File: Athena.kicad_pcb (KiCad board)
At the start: 2 copper layers, 60 x 80 mm, 81 parts, among them J1 LUM 1503-09, J2 LUM 1503-09, J3 LUM 1503-09, J4 NRJ6HF, J5 DC BU21 90, SW1 MS 500FVT, U1 NE5532, U2 TL072, U3 OPA2134, U4 NE5532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

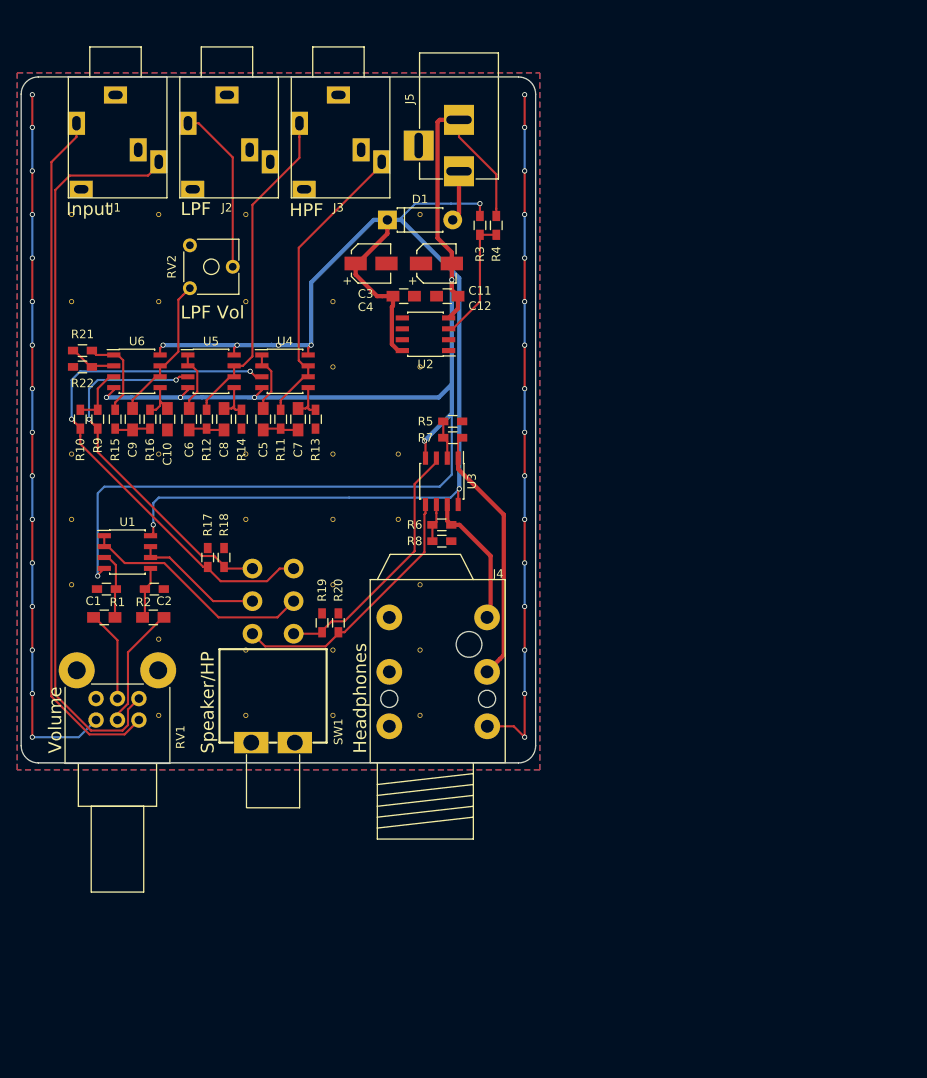
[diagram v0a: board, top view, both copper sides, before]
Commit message: changed enclosure, added power leds, resized pcb
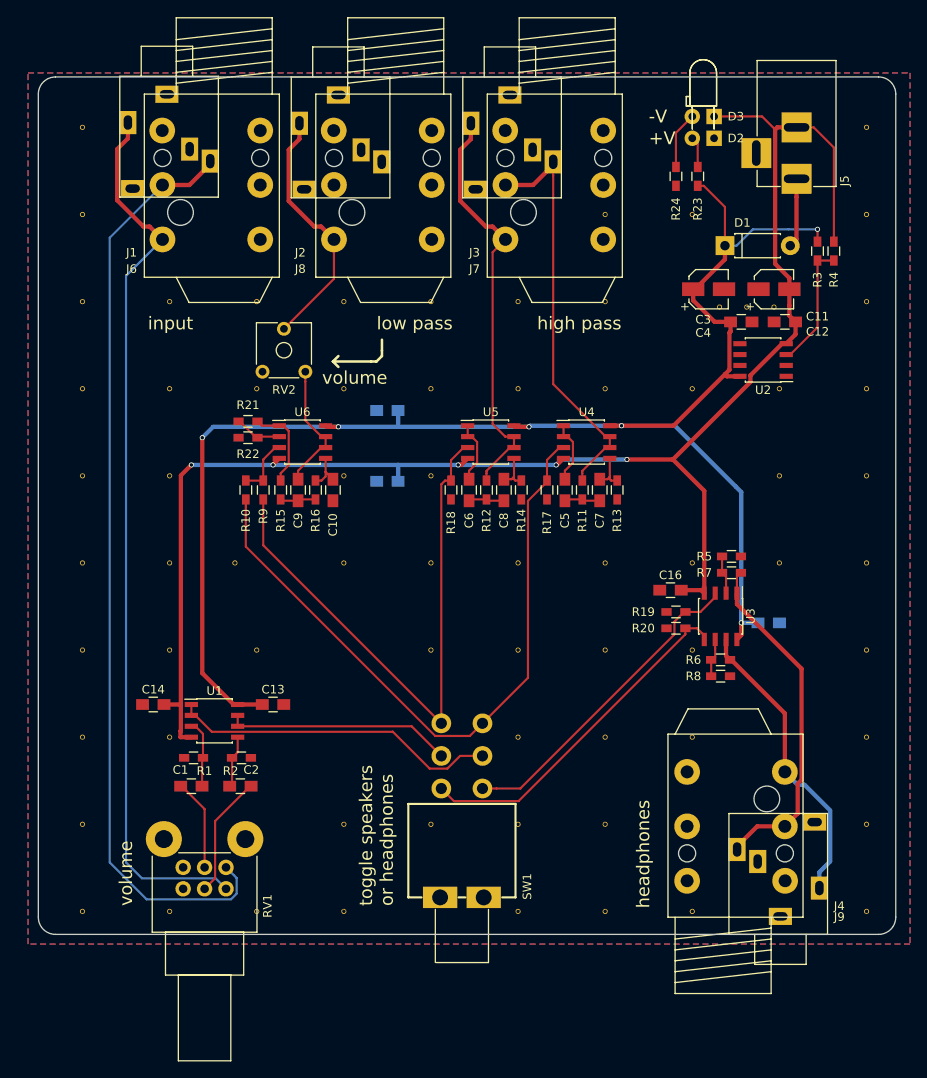
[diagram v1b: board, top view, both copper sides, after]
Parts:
- removed the REF*** at (47.0, 72.4)
- removed the V30 at (52.1, 109.2)
- added C13: 100n, Capacitors_SMD:C_0805_HandSoldering, F.Cu at (65.4, 108.0)
- added C14: 100n, Capacitors_SMD:C_0805_HandSoldering, F.Cu at (51.4, 108.0)
- added C15: 100n, Capacitors_SMD:C_0805_HandSoldering, B.Cu at (123.2, 98.4)
- added C16: 100n, Capacitors_SMD:C_0805_HandSoldering, F.Cu at (111.8, 94.6)
- added C17: 100n, Capacitors_SMD:C_0805_HandSoldering, B.Cu at (78.7, 73.7)
- added C18: 100n, Capacitors_SMD:C_0805_HandSoldering, B.Cu at (78.7, 81.9)
- added D2: LED, LEDs:LED_D3.0mm_Horizontal_O3.81mm_Z6.0mm, F.Cu at (116.8, 41.9)
- added D3: LED, LEDs:LED_D3.0mm_Horizontal_O1.27mm_Z2.0mm, F.Cu at (116.8, 39.4)
- added J6: NRJ6HF, NRJ6HF:NRJ6HF, F.Cu at (59.7, 36.8)
- added J7: NRJ6HF, NRJ6HF:NRJ6HF, F.Cu at (99.7, 36.8)
- added J8: NRJ6HF, NRJ6HF:NRJ6HF, F.Cu at (79.7, 36.8)
- added J9: LUM 1503-09, Lumberg:LUM1503-09, F.Cu at (124.6, 134.8)
- added R23: 330R, Resistors_SMD:R_0603_HandSoldering, F.Cu at (114.9, 46.4)
- added R24: 330R, Resistors_SMD:R_0603_HandSoldering, F.Cu at (112.4, 46.4)
- added REF***: OSHW-Logo2_14.6x12mm_SilkScreen, Symbols:OSHW-Logo2_14.6x12mm_SilkScreen, B.Cu at (88.0, 84.8)
- added V30: VIA, via:VIA-0.6, F.Cu at (43.2, 40.6)
- added V30: VIA, via:VIA-0.6, F.Cu at (134.6, 101.6)
- added V30: VIA, via:VIA-0.6, F.Cu at (134.6, 91.4)
- added V30: VIA, via:VIA-0.6, F.Cu at (124.5, 91.4)
- added V30: VIA, via:VIA-0.6, F.Cu at (43.2, 50.8)
- added V30: VIA, via:VIA-0.6, F.Cu at (104.1, 50.8)
- added V30: VIA, via:VIA-0.6, F.Cu at (114.3, 50.8)
- added V30: VIA, via:VIA-0.6, F.Cu at (134.6, 40.6)
- added V30: VIA, via:VIA-0.6, F.Cu at (134.6, 50.8)
- added V30: VIA, via:VIA-0.6, F.Cu at (134.6, 61.0)
- added V30: VIA, via:VIA-0.6, F.Cu at (134.6, 71.1)
- added V30: VIA, via:VIA-0.6, F.Cu at (134.6, 81.3)
- added V31: VIA, via:VIA-0.6, F.Cu at (43.2, 101.6)
- added V32: VIA, via:VIA-0.6, F.Cu at (53.3, 101.6)
- added V33: VIA, via:VIA-0.6, F.Cu at (63.5, 101.6)
- added V34: VIA, via:VIA-0.6, F.Cu at (83.8, 101.6)
- added V35: VIA, via:VIA-0.6, F.Cu at (94.0, 101.6)
- added V36: VIA, via:VIA-0.6, F.Cu at (104.1, 101.6)
- added V37: VIA, via:VIA-0.6, F.Cu at (114.3, 101.6)
- added V38: VIA, via:VIA-0.6, F.Cu at (43.2, 111.8)
- added V39: VIA, via:VIA-0.6, F.Cu at (53.3, 111.8)
- added V40: VIA, via:VIA-0.6, F.Cu at (117.5, 61.6)
- added V41: VIA, via:VIA-0.6, F.Cu at (120.7, 61.6)
- added V42: VIA, via:VIA-0.6, F.Cu at (94.0, 111.8)
- added V43: VIA, via:VIA-0.6, F.Cu at (104.1, 111.8)
- added V44: VIA, via:VIA-0.6, F.Cu at (114.3, 111.8)
- added V45: VIA, via:VIA-0.6, F.Cu at (123.8, 61.6)
- added V46: VIA, via:VIA-0.6, F.Cu at (43.2, 121.9)
- added V47: VIA, via:VIA-0.6, F.Cu at (73.7, 121.9)
- added V48: VIA, via:VIA-0.6, F.Cu at (83.8, 121.9)
- added V49: VIA, via:VIA-0.6, F.Cu at (94.0, 121.9)
- added V50: VIA, via:VIA-0.6, F.Cu at (104.1, 121.9)
- added V51: VIA, via:VIA-0.6, F.Cu at (43.2, 132.1)
- added V52: VIA, via:VIA-0.6, F.Cu at (53.3, 132.1)
- added V53: VIA, via:VIA-0.6, F.Cu at (63.5, 132.1)
- added V54: VIA, via:VIA-0.6, F.Cu at (73.7, 132.1)
- added V55: VIA, via:VIA-0.6, F.Cu at (94.0, 132.1)
- added V56: VIA, via:VIA-0.6, F.Cu at (104.1, 132.1)
- added V57: VIA, via:VIA-0.6, F.Cu at (114.3, 132.1)
- added V58: VIA, via:VIA-0.6, F.Cu at (134.6, 132.1)
- added V59: VIA, via:VIA-0.6, F.Cu at (134.6, 121.9)
- added V60: VIA, via:VIA-0.6, F.Cu at (134.6, 111.8)
- moved V29 73.0 mm to (124.5, 71.1)
- moved V28 65.5 mm to (124.5, 81.3)
- moved V7 65.3 mm to (104.1, 61.0)
- moved V26 49.6 mm to (114.3, 71.1)
- moved V12 47.7 mm to (83.8, 71.1)
- moved V27 45.5 mm to (114.3, 91.4)
- moved REF*** 43.8 mm to (88.0, 96.5)
- moved V15 41.4 mm to (43.2, 81.3)
- moved R19 41.3 mm to (112.4, 97.2), turned to 180 degrees
- moved R17 40.3 mm to (97.4, 82.9), turned to 270 degrees
- moved C11 39.5 mm to (123.8, 59.5)
- moved C12 39.5 mm to (125.1, 63.3)
- moved C3 39.5 mm to (116.2, 59.5)
- moved C4 39.5 mm to (120.0, 63.3)
- moved D1 39.5 mm to (118.1, 54.4)
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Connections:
- J2 pad 2: (no net) -> Net-(J2-Pad2)
- J2 pad 4: (no net) -> Net-(J2-Pad4)
- J2 pad 5: (no net) -> Net-(J2-Pad5)
- J3 pad 4: (no net) -> Net-(J3-Pad4)
- J3 pad 5: (no net) -> Net-(J3-Pad5)
- J4 pad 4: (no net) -> Net-(J4-Pad4)
- J4 pad 5: (no net) -> Net-(J4-Pad5)
- J4 pad 6: (no net) -> Net-(J4-Pad6)
- J5 pad 3: (no net) -> Net-(J5-Pad3)
- RV1 pad 0: (no net) -> GND
- SW1 pad : (no net) -> GND
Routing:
- net GND: track 162.6 -> 0.00 mm, vias 32 -> 0
- net +6V: track 152.2 -> 187.0 mm, vias 7 -> 6
- net IN_SPK_L: track 43.8 -> 68.8 mm, vias 2 -> 0
- net Net-(J1-Pad1): track 80.8 -> 104.1 mm
- net -6V: track 167.7 -> 190.3 mm, vias 6 -> 5
- net Net-(J1-Pad2): track 86.6 -> 108.9 mm
- net HP_L: track 15.8 -> 35.4 mm
- net IN_SPK_R: track 63.0 -> 79.2 mm, vias 2 -> 0
- net TOP_R: track 35.7 -> 49.2 mm
- net Net-(SW1-Pad5): track 15.7 -> 26.5 mm
- net HP_R: track 31.0 -> 41.1 mm
- net IN_HP_L: track 31.6 -> 41.5 mm
- net SUB: track 19.6 -> 29.6 mm
- net TOP_L: track 39.3 -> 49.2 mm
- net Net-(SW1-Pad2): track 29.1 -> 37.9 mm
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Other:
- board size 60 x 80 mm -> 100 x 100 mm
- board text added: "+V"
- board text added: "-V"
- board text added: "headphones"
- board text added: "high pass"
- board text added: "input"
- board text added: "low pass"
- board text added: "toggle speakers or headphones"
- board text added: "volume"
- board text removed: "HPF"
- board text removed: "Headphones"
- board text removed: "Input"
- board text removed: "LPF"
- board text removed: "LPF Vol"
- board text removed: "Speaker/HP"
- board text removed: "Volume"
